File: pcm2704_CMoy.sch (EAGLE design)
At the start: 85 parts, among them IC3 7815DT, IC4 tsr 1-2433, IC5 7915TV, Q1 12MHz, U1 PCM2704, U2 OPA2134P, U3 TC962EPA, X2 PN61729-S, X5 22-23-2031, X6 22-23-2031

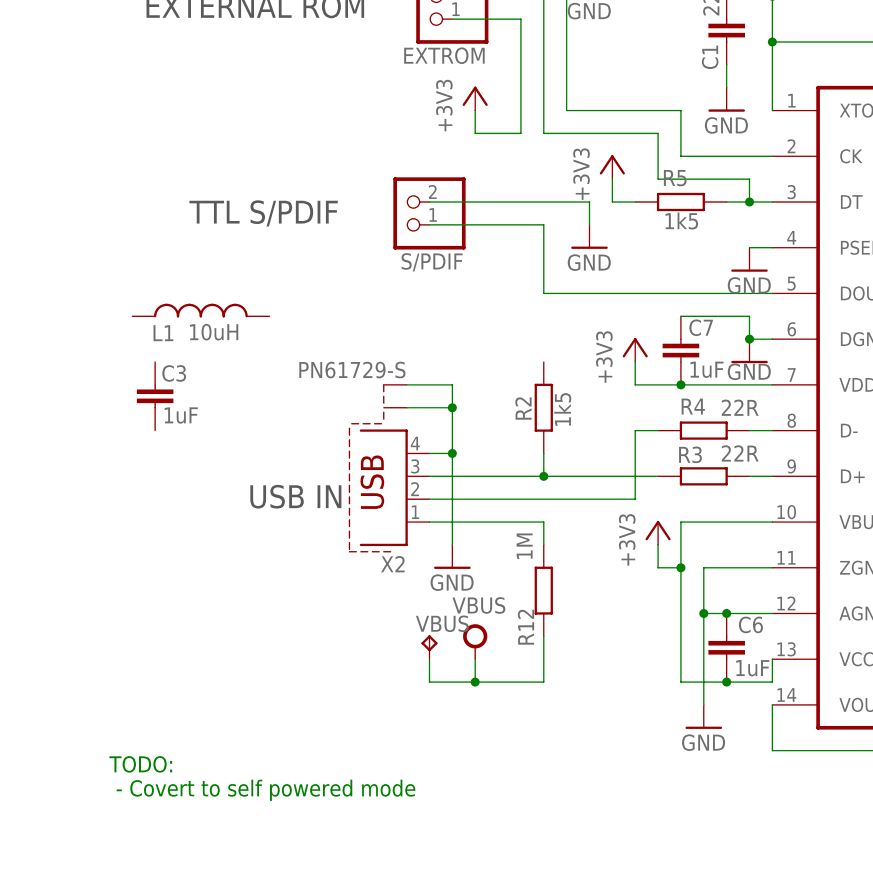
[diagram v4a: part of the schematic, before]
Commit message: - Added D+ pullup activator transistor
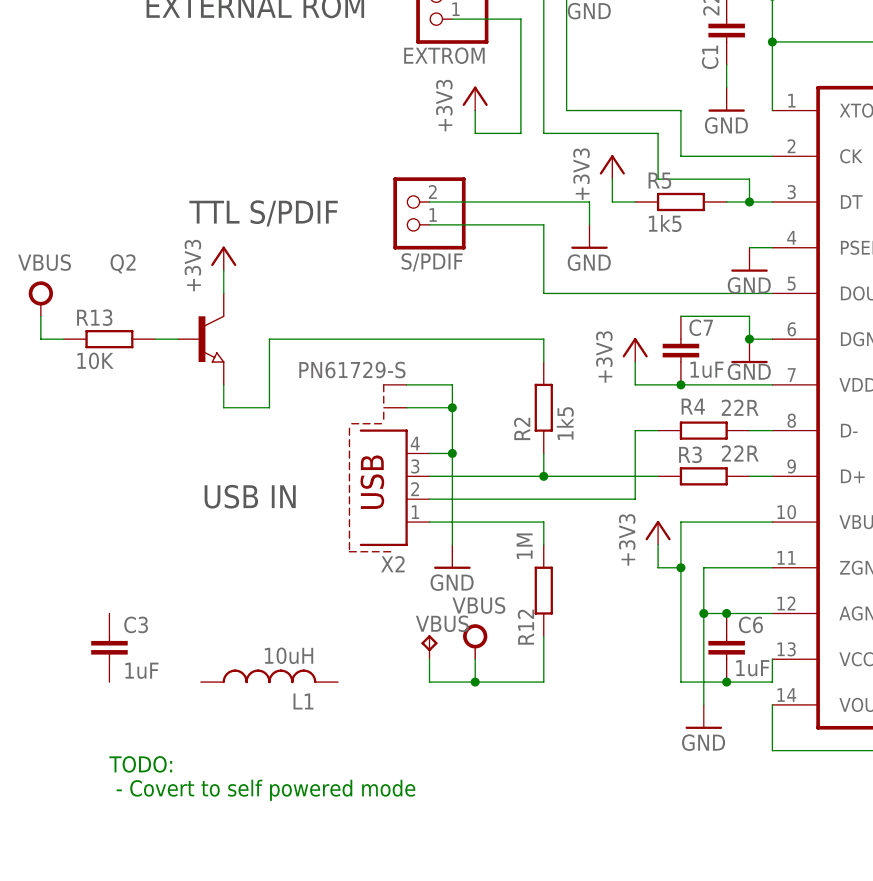
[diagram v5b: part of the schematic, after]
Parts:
- added Q2: (no value), semicon-smd-ipc:NPN-TRANSISTOR_SOT23
- added R13: 10K, rcl:R-EU_R0805
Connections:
- new net N$38: Q2.B, R13.2
- new net N$39: Q2.E, R2.2
- net +3V3: now also Q2.C
- net VBUS: now also R13.1
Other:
- moved on the sheet: C3, L1
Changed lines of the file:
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@@
 <part name="R12" library="rcl" deviceset="R-EU_" device="M0805" value="1M"/>
 <part name="+3V8" library="supply1" deviceset="+3V3" device=""/>
+<part name="Q2" library="semicon-smd-ipc" deviceset="NPN-TRANSISTOR_" device="SOT23"/>
+<part name="V3" library="supply" deviceset="VBUS" device=""/>
+<part name="R13" library="rcl" deviceset="R-EU_" device="R0805" value="10K"/>
+<part name="+3V9" library="supply1" deviceset="+3V3" device=""/>
 </parts>
 <sheets>
@@
 <plain>
 <text x="144.78" y="68.58" size="2.54" layer="97" font="vector">LINE OUT</text>
-<text x="-20.1783" y="62.5068" size="2.54" layer="97" font="vector">USB IN</text>
+<text x="-25.2583" y="62.5068" size="2.54" layer="97" font="vector">USB IN</text>
 <text x="5.08" y="134.62" size="5.08" layer="97" font="vector">PCM2704 USB DAC</text>
 <text x="-26.6645" y="94.1219" size="2.54" layer="97">TTL S/PDIF</text>
@@
 <attribute name="VALUE" x="64.2365" y="115.5384" size="1.778" layer="96"/>
 </instance>
-<instance part="R2" gate="G$1" x="12.7" y="73.66" smashed="yes" rot="R90">
-<attribute name="NAME" x="11.3433" y="72.1176" size="1.778" layer="95" rot="R90"/>
-<attribute name="VALUE" x="15.7183" y="71.409" size="1.778" layer="96" rot="R90"/>
-</instance>
+<instance part="R2" gate="G$1" x="12.7" y="73.66" rot="R90"/>
 <instance part="R4" gate="G$1" x="30.48" y="71.12" smashed="yes">
 <attribute name="NAME" x="27.8038" y="72.9024" size="1.778" layer="95"/>
@@
 <attribute name="VALUE" x="91.5741" y="116.9927" size="1.778" layer="96" rot="R90"/>
 </instance>
-<instance part="C3" gate="G$1" x="-30.48" y="76.2" smashed="yes">
-<attribute name="NAME" x="-29.8064" y="76.581" size="1.778" layer="95"/>
-<attribute name="VALUE" x="-29.6646" y="71.9267" size="1.778" layer="96"/>
+<instance part="C3" gate="G$1" x="-35.56" y="48.26" smashed="yes">
+<attribute name="NAME" x="-34.036" y="48.641" size="1.778" layer="95"/>
+<attribute name="VALUE" x="-34.036" y="43.561" size="1.778" layer="96"/>
 </instance>
 <instance part="C4" gate="G$1" x="96.52" y="63.5" rot="R180"/>
@@
 <instance part="GND7" gate="1" x="88.9" y="106.68"/>
 <instance part="GND8" gate="1" x="96.52" y="45.72"/>
-<instance part="R5" gate="G$1" x="27.94" y="96.52" smashed="yes">
-<attribute name="NAME" x="25.8307" y="98.3023" size="1.778" layer="95"/>
-<attribute name="VALUE" x="25.9725" y="93.5018" size="1.778" layer="96"/>
-</instance>
+<instance part="R5" gate="G$1" x="27.94" y="96.52"/>
 <instance part="GND9" gate="1" x="147.32" y="30.48"/>
-<instance part="L1" gate="G$1" x="-25.4" y="83.82" smashed="yes" rot="R90">
-<attribute name="NAME" x="-28.2568" y="82.8338" size="1.778" layer="95" rot="R180"/>
-<attribute name="VALUE" x="-21.0287" y="82.9477" size="1.778" layer="96" rot="R180"/>
-</instance>
+<instance part="L1" gate="G$1" x="-17.78" y="43.18" rot="R90"/>
 <instance part="GND11" gate="1" x="17.78" y="91.44"/>
 <instance part="GND2" gate="1" x="101.6" y="71.12"/>
@@
 </instance>
 <instance part="+3V8" gate="G$1" x="5.08" y="109.22"/>
+<instance part="Q2" gate="G$1" x="-25.4" y="81.28"/>
+<instance part="V3" gate="G$1" x="-43.18" y="86.36"/>
+<instance part="R13" gate="G$1" x="-35.56" y="81.28"/>
+<instance part="+3V9" gate="G$1" x="-22.86" y="91.44"/>
 </instances>
 <busses>
@@
 <wire x1="5.08" y1="45.72" x2="5.08" y2="43.18" width="0.1524" layer="91"/>
 <junction x="5.08" y="43.18"/>
+</segment>
+<segment>
+<pinref part="V3" gate="G$1" pin="VBUS"/>
+<pinref part="R13" gate="G$1" pin="1"/>
+<wire x1="-43.18" y1="83.82" x2="-43.18" y2="81.28" width="0.1524" layer="91"/>
+<wire x1="-43.18" y1="81.28" x2="-40.64" y2="81.28" width="0.1524" layer="91"/>
 </segment>
 </net>
@@
 <wire x1="5.08" y1="104.14" x2="5.08" y2="106.68" width="0.1524" layer="91"/>
 </segment>
+<segment>
+<pinref part="Q2" gate="G$1" pin="C"/>
+<pinref part="+3V9" gate="G$1" pin="+3V3"/>
+<wire x1="-22.86" y1="86.36" x2="-22.86" y2="88.9" width="0.1524" layer="91"/>
+</segment>
 </net>
 <net name="SUSPEND" class="0">
@@
 </segment>
 </net>
+<net name="N$38" class="0">
+<segment>
+<pinref part="R13" gate="G$1" pin="2"/>
+<pinref part="Q2" gate="G$1" pin="B"/>
+<wire x1="-30.48" y1="81.28" x2="-27.94" y2="81.28" width="0.1524" layer="91"/>
+</segment>
+</net>
+<net name="N$39" class="0">
+<segment>
+<pinref part="Q2" gate="G$1" pin="E"/>
+<wire x1="-22.86" y1="76.2" x2="-22.86" y2="73.66" width="0.1524" layer="91"/>
+<wire x1="-22.86" y1="73.66" x2="-17.78" y2="73.66" width="0.1524" layer="91"/>
+<wire x1="-17.78" y1="73.66" x2="-17.78" y2="81.28" width="0.1524" layer="91"/>
+<wire x1="-17.78" y1="81.28" x2="12.7" y2="81.28" width="0.1524" layer="91"/>
+<pinref part="R2" gate="G$1" pin="2"/>
+<wire x1="12.7" y1="81.28" x2="12.7" y2="78.74" width="0.1524" layer="91"/>
+</segment>
+</net>

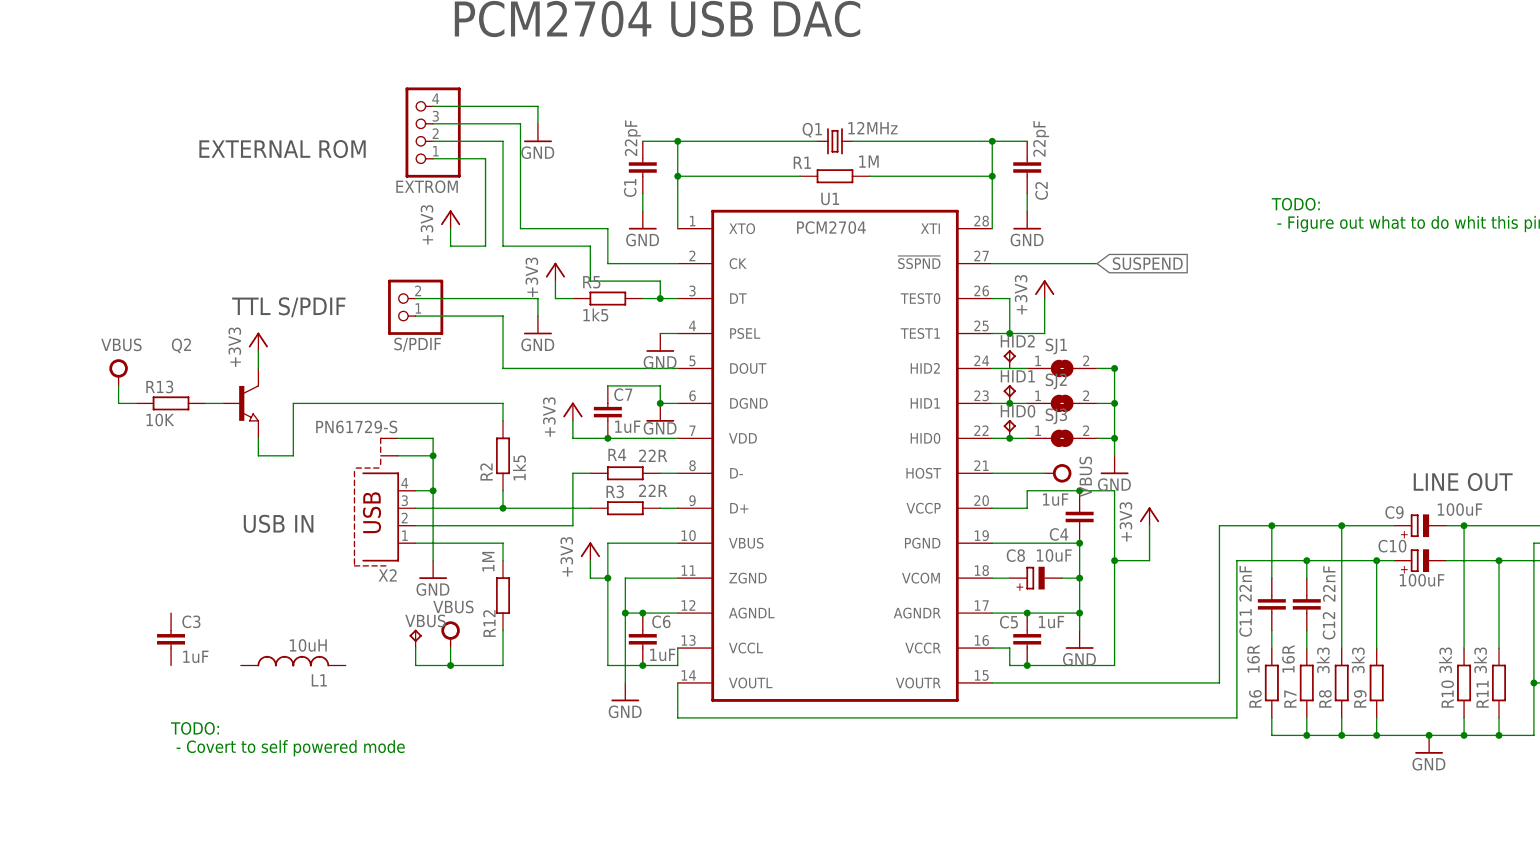
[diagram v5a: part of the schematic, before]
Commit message: - Modified capacitor names to match the datasheet example (DAC)
 - Fixed a few capacitor values that did not match the datasheet example (DAC)
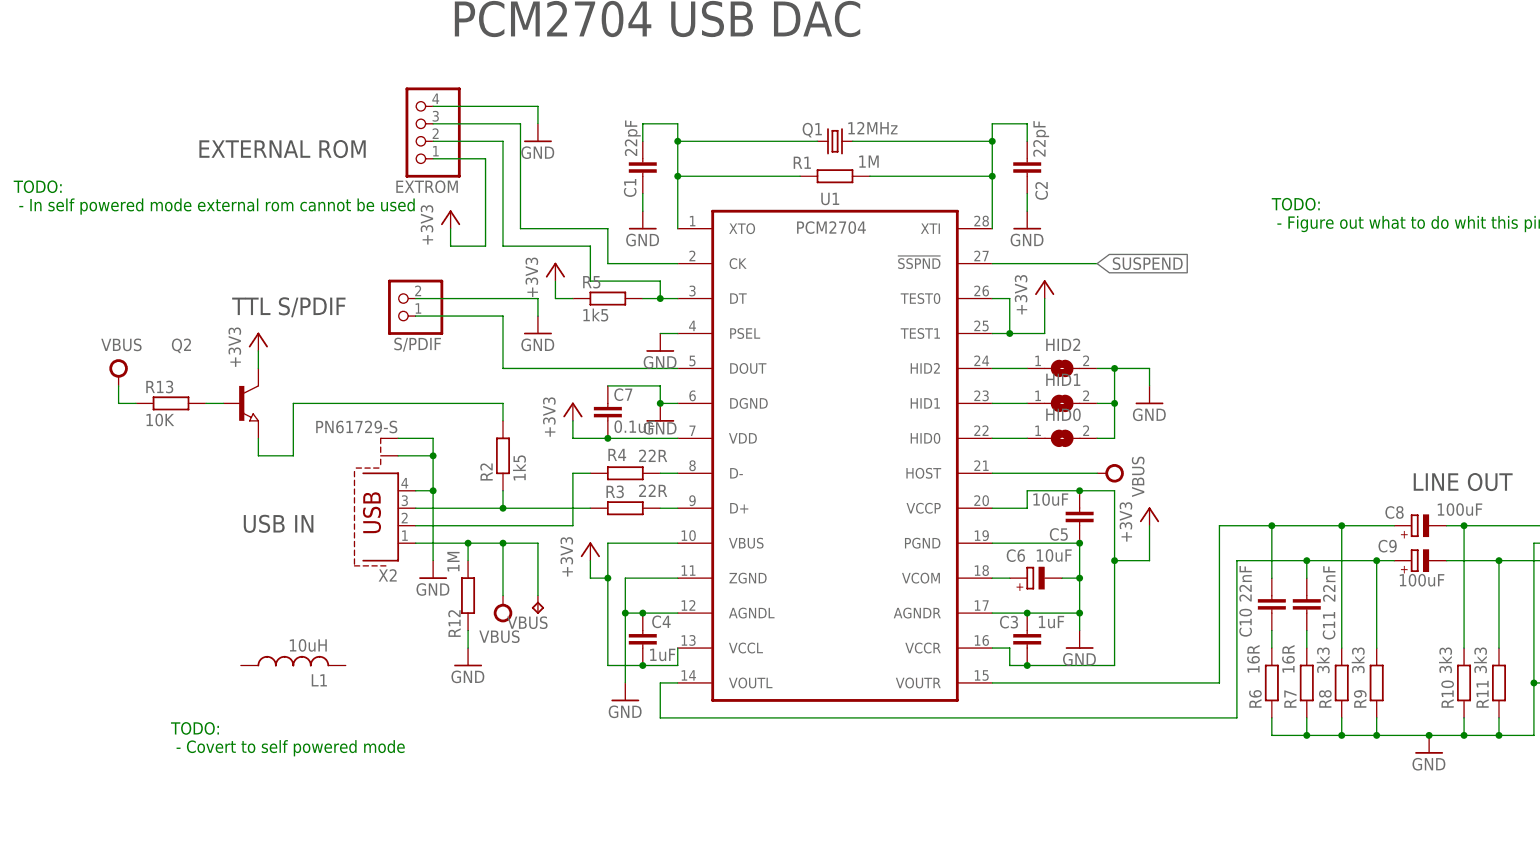
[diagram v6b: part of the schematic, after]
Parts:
- removed C12: 22nF, rcl:C-EU050-025X075
- removed SJ1, SJ2, SJ3: (no value), jumper:SJ
- C10: value 100uF -> 22nF; device rcl:CPOL-EUE3.5-10 -> rcl:C-EU050-025X075
- C5: value 1uF -> 10uF
- C6: value 1uF -> 10uF; device rcl:C-EUC0805 -> rcl:CPOL-EUE2.5-7
- C7: value 1uF -> 0.1uF
- C8: value 10uF -> 100uF; device rcl:CPOL-EUE2.5-7 -> rcl:CPOL-EUE3.5-10
- HID0, HID1, HID2: value TPTP20R -> (none); device testpad:TPTP20R -> jumper:SJ
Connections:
- removed net N$2: R12.2, X2.1
- net +3V3: now also C3.1, C5.2; no longer C5.1, C6.2
- net DAC_OUT_LEFT: now also C9.-; no longer C10.-
- net DAC_OUT_RIGHT: now also C8.-; no longer C9.-
- net GND: now also C3.2, C5.1, C6.-, HID0.2, HID1.2, HID2.2, R12.1; no longer C5.2, C6.1, C8.-, SJ1.2, SJ2.2, SJ3.2
- net N$12: now also HID2.1; no longer HID2.TP, SJ1.1
- net N$15: now also HID1.1; no longer HID1.TP, SJ2.1
- net N$16: now also HID0.1; no longer HID0.TP, SJ3.1
- net N$26: now also C10.2; no longer C11.2
- net N$27: now also C11.2; no longer C12.2
- net N$28: now also C10.1, C8.+; no longer C11.1, C9.+
- net N$29: now also C11.1, C9.+; no longer C10.+, C12.1
- net VBUS: now also R12.2, X2.1; no longer R12.1
- net VCOM: now also C6.+; no longer C8.+
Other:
- note added: "TODO: - In self powered mode external rom cannot be used"
- moved on the sheet: C11, C3, C4, C5, C8, C9, R12, VBUS

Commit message: - Removed the external rom connector, because it does not support descriptor overwriting in self powered mode
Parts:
- removed EXTROM: (no value), pinhead:PINHD-1X4
- added CK, DT: TPTP20R, testpad:TPTP20R
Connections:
- net +3V3: no longer EXTROM.1
- net GND: no longer EXTROM.4
- net N$20: now also DT.TP; no longer EXTROM.2
- net N$9: now also CK.TP; no longer EXTROM.3
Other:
- note added: "DONE: - Covert to self powered mode"
- note added: "DONE: - Create part for the pj325 jack connector - Replace this jack for the pj325 https://i.stack.imgur.com/eo183.png"
- note added: "DONE: - Remove old (virtual ground) power source"
- note added: "DONE: - Replace pot with Alps RK097"
- note removed: "EXTERNAL ROM"
- note removed: "TODO: - Covert to self powered mode"
- note removed: "TODO: - Create part for the pj325 jack connector - Replace this jack for the pj325 https://i.stack.imgur.com/eo183.png"
- note removed: "TODO: - In self powered mode external rom cannot be used"
- note removed: "TODO: - Remove old (virtual ground) power source"
- note removed: "TODO: - Replace pot with Alps RK097"
- moved on the sheet: -15V, C13, C22, C23, C24, C25, FREQX2, IC5, U3

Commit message: - Cosmetics
 - Added bus power indicator led
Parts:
- removed S1: (no value), switch:LPV-1
- added LED2: (no value), led:LED3MM
- added R14: 470R, rcl:R-EU_0204/7
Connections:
- new net N$2: LED2.A, R14.2
- net GND: now also LED2.C
- net VBUS: now also R14.1
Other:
- note added: "BUS POWER INDICATOR LED"
- note added: "DONE: - add reverse polarity protection diode (note the voltage drop!) - add polyfuse - 15v+ Vsource - add lm7812/15 positive rail stab - add lm7912/15 negative rail stab - add TC962 for negative rail (LTC1044, SI7661, ICL7662) Note: most of this needs to be smd, otherwise it might not fit the case"
- note added: "TODO if the SMPS is noisy: - add zener diode to drop Vsource to 4-5V - add lm7833 for 3.3v rail"
- note removed: "TODO: - add reverse polarity protection diode (note the voltage drop!) - add polyfuse - 15v+ Vsource - add lm7812/15 positive rail stab - add lm7912/15 negative rail stab - add zener diode to drop Vsource to 4-5V - add lm7833 for 3.3v rail - add TC962 for negative rail (LTC1044, SI7661, ICL7662) Note: most of this needs to be smd, otherwise it might not fit the case"
- moved on the sheet: -15V, 15V, C13, C14, C15, C18, C21, C22, C23, C24, C25, D1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
